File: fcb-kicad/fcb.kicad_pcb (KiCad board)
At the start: 4 copper layers, 45 x 45 mm, 92 parts, among them J1 Conn_ESC_4in1, J10 PH1X3, J11 PH1X3, J2 SWD, J3 Conn_Coaxial, J4 PH1X4, J5 USB_B_Micro, J6 PH1X3, J7 PH1X3, J8 PH1X4, J9 PH1X3, Q1 S8050 J3Y, SW1 SW_Push, SW2 SW_Push, T1 JLCPCB_NPTH, T2 JLCPCB_NPTH, T3 JLCPCB_NPTH, U1 STM32F411CEUx, U2 TPS5430DDA, U3 AMS1117-3.3, U4 W25Q128JVS, U5 LSM6DS3, U6 DL-RTS4432, U7 DPS310, U8 QMC5883L, U9 SRV05-4, Y1 16 MHz

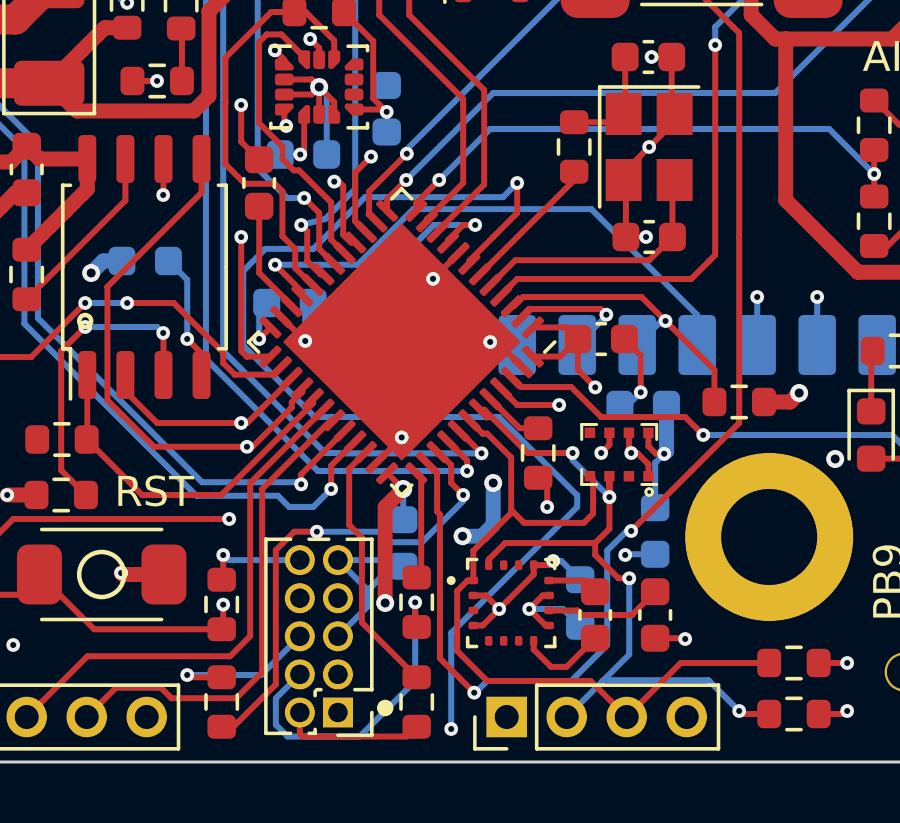
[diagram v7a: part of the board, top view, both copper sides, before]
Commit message: wider pads for barometer footprint
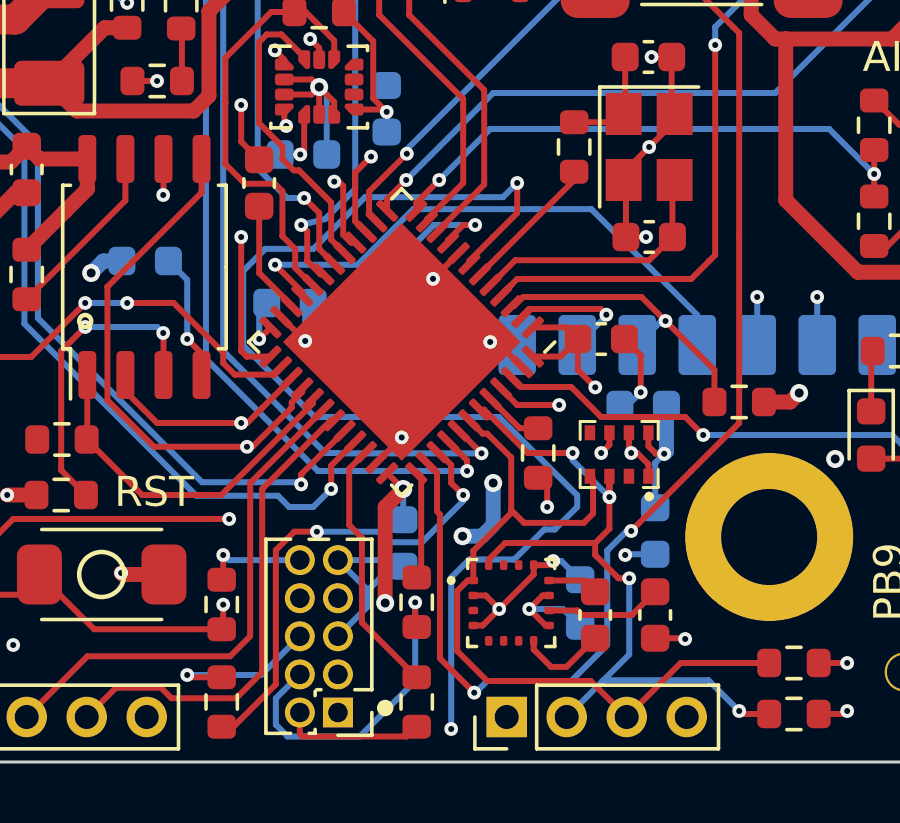
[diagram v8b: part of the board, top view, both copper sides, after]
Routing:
- net CPU_NRST: track 59.9 -> 61.0 mm
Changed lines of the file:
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@@
     (solder_mask_min_width 0.15)
     (aux_axis_origin 125.5 79.5)
+    (grid_origin 125.5 79.5)
     (pcbplotparams
       (layerselection 0x00010fc_ffffffff)
@@
       (effects (font (size 1 1) (thickness 0.15)))
     )
-    (fp_line (start 1 -0.75) (end 1 -1.25) (layer "F.SilkS") (width 0.1))
-    (fp_line (start -1 1.25) (end -0.5 1.25) (layer "F.SilkS") (width 0.1))
-    (fp_line (start 1 1.25) (end 1 0.75) (layer "F.SilkS") (width 0.1))
-    (fp_line (start 0.5 1.25) (end 1 1.25) (layer "F.SilkS") (width 0.1))
-    (fp_line (start -1 -1.25) (end -1 -0.75) (layer "F.SilkS") (width 0.1))
-    (fp_line (start -0.5 -1.25) (end -1 -1.25) (layer "F.SilkS") (width 0.1))
-    (fp_line (start -1 0.75) (end -1 1.25) (layer "F.SilkS") (width 0.1))
-    (fp_circle (center 1.25 -1) (end 1.3 -1.1) (layer "F.SilkS") (width 0.1) (fill none))
+    (fp_line (start 1.1 1.3) (end 1.1 0.8) (layer "F.SilkS") (width 0.1))
+    (fp_line (start 1.1 -1.3) (end 1.1 -0.8) (layer "F.SilkS") (width 0.1))
+    (fp_line (start 0.5 1.3) (end 1.1 1.3) (layer "F.SilkS") (width 0.1))
+    (fp_line (start -1.1 -1.3) (end -1.1 -0.75) (layer "F.SilkS") (width 0.1))
+    (fp_line (start -0.5 -1.3) (end -1.1 -1.3) (layer "F.SilkS") (width 0.1))
+    (fp_line (start 0.5 -1.3) (end 1.1 -1.3) (layer "F.SilkS") (width 0.1))
+    (fp_line (start -1.1 1.3) (end -0.5 1.3) (layer "F.SilkS") (width 0.1))
+    (fp_line (start -1.1 0.8) (end -1.1 1.3) (layer "F.SilkS") (width 0.1))
+    (fp_circle (center 1.4 -1) (end 1.511803 -1) (layer "F.SilkS") (width 0.1) (fill solid))
     (fp_rect (start -1 -1.25) (end 1 1.25) (layer "Dwgs.User") (width 0.05) (fill none))
     (fp_rect (start 1.25 -1.5) (end -1.25 1.5) (layer "F.CrtYd") (width 0.05) (fill none))
     (fp_rect (start -1 -1.25) (end 1 1.25) (layer "F.Fab") (width 0.05) (fill none))
-    (pad "1" smd rect (at 0.725 -0.975 90) (size 0.35 0.35) (layers "F.Cu" "F.Paste" "F.Mask")
+    (pad "1" smd rect (at 0.725 -0.975 90) (size 0.5 0.35) (layers "F.Cu" "F.Paste" "F.Mask")
       (net 65 "GND") (pinfunction "GND") (pintype "power_in"))
-    (pad "2" smd rect (at 0.725 -0.325 90) (size 0.35 0.35) (layers "F.Cu" "F.Paste" "F.Mask")
+    (pad "2" smd rect (at 0.725 -0.325 90) (size 0.5 0.35) (layers "F.Cu" "F.Paste" "F.Mask")
       (net 58 "unconnected-(U7-Pad2)") (pinfunction "CSB") (pintype "input+no_connect"))
-    (pad "3" smd rect (at 0.725 0.325 90) (size 0.35 0.35) (layers "F.Cu" "F.Paste" "F.Mask")
+    (pad "3" smd rect (at 0.725 0.325 90) (size 0.5 0.35) (layers "F.Cu" "F.Paste" "F.Mask")
       (net 50 "I2C1_SDA") (pinfunction "SDI") (pintype "bidirectional"))
-    (pad "4" smd rect (at 0.725 0.975 90) (size 0.35 0.35) (layers "F.Cu" "F.Paste" "F.Mask")
+    (pad "4" smd rect (at 0.725 0.975 90) (size 0.5 0.35) (layers "F.Cu" "F.Paste" "F.Mask")
       (net 49 "I2C1_SCL") (pinfunction "SCK") (pintype "input"))
-    (pad "5" smd rect (at -0.725 0.975 90) (size 0.35 0.35) (layers "F.Cu" "F.Paste" "F.Mask")
+    (pad "5" smd rect (at -0.725 0.975 90) (size 0.5 0.35) (layers "F.Cu" "F.Paste" "F.Mask")
       (net 74 "unconnected-(U7-Pad5)") (pinfunction "SDO") (pintype "bidirectional+no_connect"))
-    (pad "6" smd rect (at -0.725 0.325 90) (size 0.35 0.35) (layers "F.Cu" "F.Paste" "F.Mask")
+    (pad "6" smd rect (at -0.725 0.325 90) (size 0.5 0.35) (layers "F.Cu" "F.Paste" "F.Mask")
       (net 2 "+3V3") (pinfunction "VDDIO") (pintype "power_in"))
-    (pad "7" smd rect (at -0.725 -0.325 90) (size 0.35 0.35) (layers "F.Cu" "F.Paste" "F.Mask")
+    (pad "7" smd rect (at -0.725 -0.325 90) (size 0.5 0.35) (layers "F.Cu" "F.Paste" "F.Mask")
       (net 65 "GND") (pinfunction "GND") (pintype "power_in"))
-    (pad "8" smd rect (at -0.725 -0.975 90) (size 0.35 0.35) (layers "F.Cu" "F.Paste" "F.Mask")
+    (pad "8" smd rect (at -0.725 -0.975 90) (size 0.5 0.35) (layers "F.Cu" "F.Paste" "F.Mask")
       (net 2 "+3V3") (pinfunction "VDD") (pintype "power_in"))
   )
@@
   (segment (start 144.8 119.2545) (end 144.8 121.8) (width 0.2) (layer "In2.Cu") (net 16))
   (segment (start 144.8 121.8) (end 146.8 123.8) (width 0.2) (layer "In2.Cu") (net 16))
-  (segment (start 154.129031 105.670969) (end 149.529031 105.670969) (width 0.2) (layer "B.Cu") (net 16))
-  (segment (start 147.851157 113) (end 153.990006 113) (width 0.2) (layer "B.Cu") (net 16))
-  (segment (start 149.529031 105.670969) (end 147.803925 107.396075) (width 0.2) (layer "B.Cu") (net 16))
-  (segment (start 145.470489 110.619332) (end 147.851157 113) (width 0.2) (layer "B.Cu") (net 16))
-  (segment (start 154.6 105.2) (end 154.129031 105.670969) (width 0.2) (layer "B.Cu") (net 16))
-  (segment (start 152.4 120.2) (end 152.4 123.4) (width 0.2) (layer "B.Cu") (net 16))
-  (segment (start 156.6 115.609994) (end 156.6 116) (width 0.2) (layer "B.Cu") (net 16))
-  (segment (start 145.470489 108.129511) (end 145.470489 110.619332) (width 0.2) (layer "B.Cu") (net 16))
-  (segment (start 153.990006 113) (end 156.6 115.609994) (width 0.2) (layer "B.Cu") (net 16))
-  (segment (start 147.803925 107.396075) (end 146.203925 107.396075) (width 0.2) (layer "B.Cu") (net 16))
-  (segment (start 156.6 116) (end 152.4 120.2) (width 0.2) (layer "B.Cu") (net 16))
-  (segment (start 146.203925 107.396075) (end 145.470489 108.129511) (width 0.2) (layer "B.Cu") (net 16))
+  (segment (start 149.529031 105.670969) (end 154.129031 105.670969) (width 0.2) (layer "B.Cu") (net 16))
+  (segment (start 156.6 115.609994) (end 153.990006 113) (width 0.2) (layer "B.Cu") (net 16))
+  (segment (start 147.851157 113) (end 145.470489 110.619332) (width 0.2) (layer "B.Cu") (net 16))
+  (segment (start 155.85 116.75) (end 156.6 116) (width 0.2) (layer "B.Cu") (net 16))
+  (segment (start 146.203925 107.396075) (end 147.803925 107.396075) (width 0.2) (layer "B.Cu") (net 16))
+  (segment (start 152.4 123.4) (end 152.4 118.35) (width 0.2) (layer "B.Cu") (net 16))
+  (segment (start 152.4 118.35) (end 153 117.75) (width 0.2) (layer "B.Cu") (net 16))
+  (segment (start 155.5 116.75) (end 155.85 116.75) (width 0.2) (layer "B.Cu") (net 16))
+  (segment (start 153 117.75) (end 154.5 117.75) (width 0.2) (layer "B.Cu") (net 16))
+  (segment (start 145.470489 108.129511) (end 146.203925 107.396075) (width 0.2) (layer "B.Cu") (net 16))
+  (segment (start 153.990006 113) (end 147.851157 113) (width 0.2) (layer "B.Cu") (net 16))
+  (segment (start 147.803925 107.396075) (end 149.529031 105.670969) (width 0.2) (layer "B.Cu") (net 16))
+  (segment (start 145.470489 110.619332) (end 145.470489 108.129511) (width 0.2) (layer "B.Cu") (net 16))
+  (segment (start 156.6 116) (end 156.6 115.609994) (width 0.2) (layer "B.Cu") (net 16))
+  (segment (start 154.5 117.75) (end 155.5 116.75) (width 0.2) (layer "B.Cu") (net 16))
+  (segment (start 154.129031 105.670969) (end 154.6 105.2) (width 0.2) (layer "B.Cu") (net 16))
   (segment (start 133.325 112.25) (end 134.9625 112.25) (width 0.2) (layer "F.Cu") (net 17))
   (segment (start 151.22 83.9185) (end 150.95 84.1885) (width 0.5) (layer "F.Cu") (net 18))
@@
       )
     )
+  )
+  (zone (net 0) (net_name "") (layer "F.Cu") (hatch edge 0.508)
+    (connect_pads (clearance 0))
+    (min_thickness 0.254)
+    (keepout (tracks allowed) (vias allowed) (pads allowed ) (copperpour not_allowed) (footprints allowed))
+    (fill (thermal_gap 0.508) (thermal_bridge_width 0.508))
+    (polygon
+      (pts
+        (xy 155.3 120.1)
+        (xy 153.5 120.1)
+        (xy 153.5 118.3)
+        (xy 155.3 118.3)
+      )
+    )
